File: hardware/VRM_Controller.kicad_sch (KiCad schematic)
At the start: 11 parts, among them U2001 TPS536C7B1RSLT

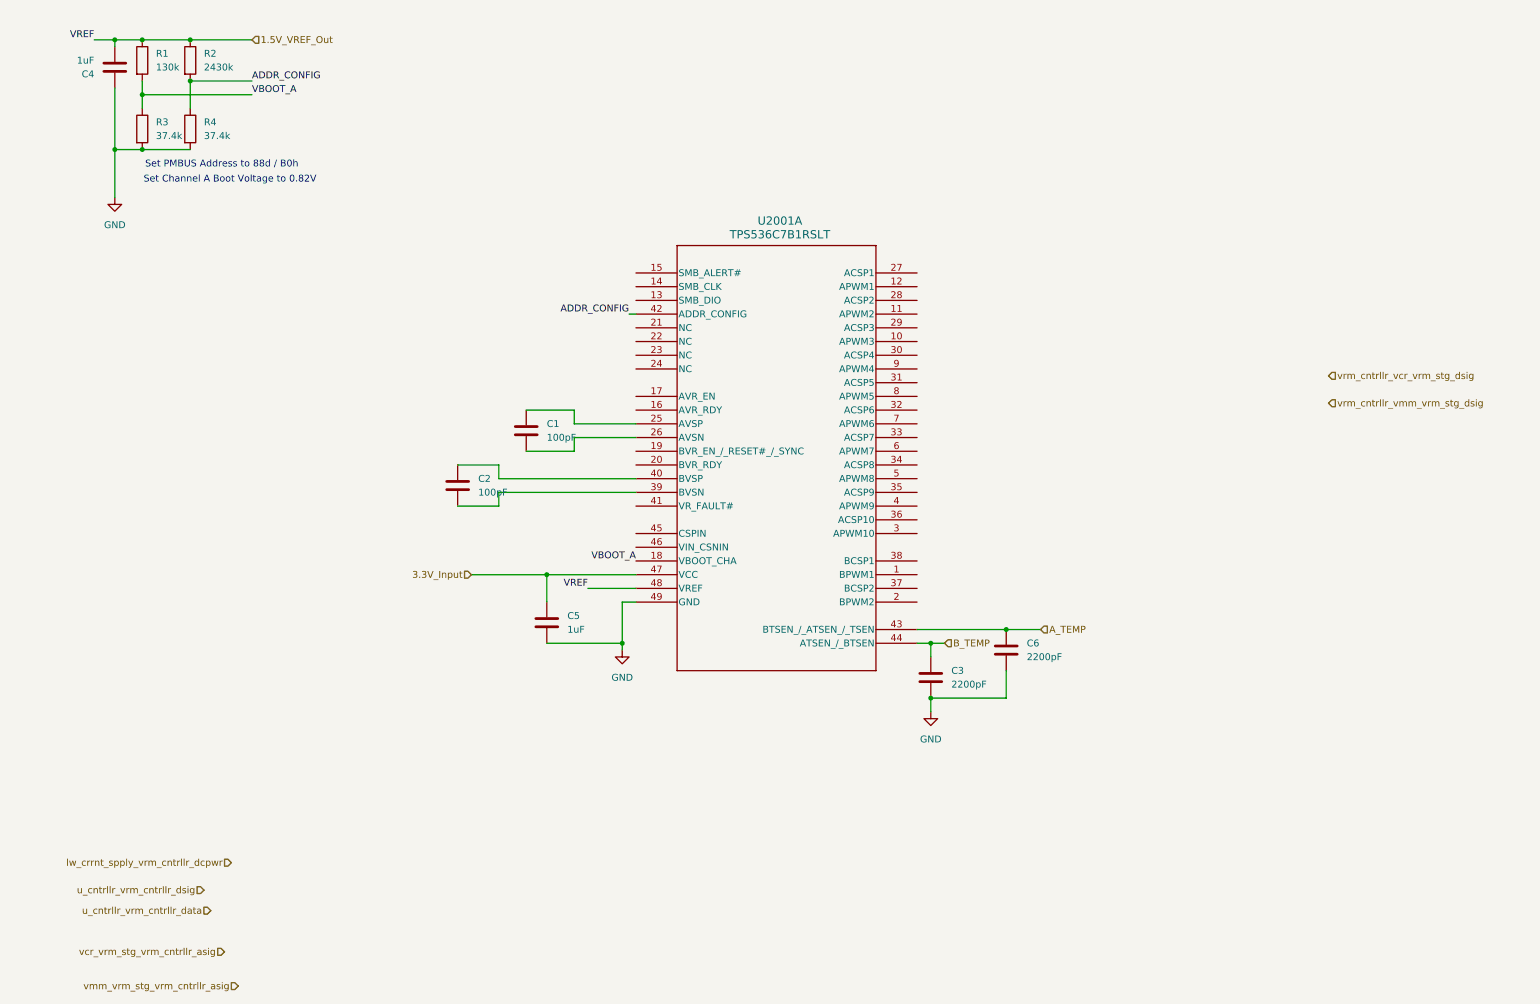
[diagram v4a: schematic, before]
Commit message: feat(schematic): VRM Controller Design
- 12v Current Sense
- Digital I/O
- MOSFET I/0
- etc
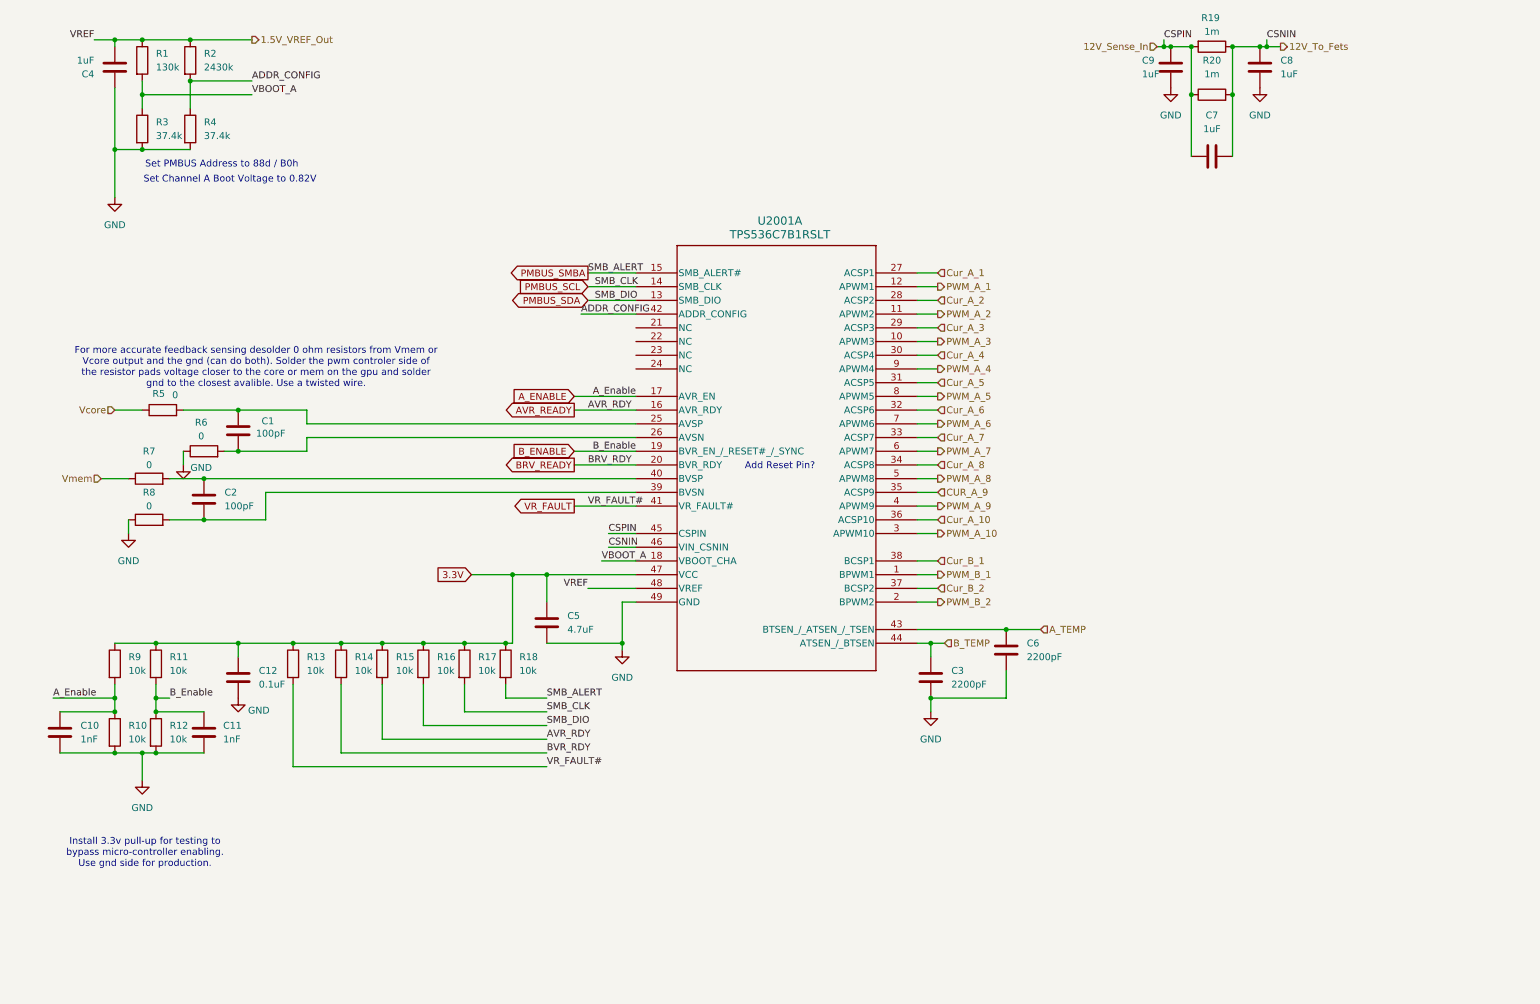
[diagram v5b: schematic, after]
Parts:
- added C10, C11: 1nF, Capacitor_SMD:C_0805_2012Metric, symbol Device:C
- added C12: 0.1uF, Capacitor_SMD:C_0805_2012Metric, symbol Device:C
- added C7, C8, C9: 1uF, Capacitor_SMD:C_0805_2012Metric, symbol Device:C
- added R10, R11, R12, R13, R14, R15, R16, R17, R18, R9: 10k, Resistor_SMD:R_0805_2012Metric, symbol Device:R
- added R19, R20: 1m, Resistor_SMD:R_Shunt_Vishay_WSK2512_6332Metric_T1.19mm, symbol Device:R
- added R5, R6, R7, R8: 0, Resistor_SMD:R_2512_6332Metric_Pad1.40x3.35mm_HandSolder, symbol Device:R
- C1, C2, C3, C4, C6: footprint (none) -> Capacitor_SMD:C_0805_2012Metric
- C5: value 1uF -> 4.7uF; footprint (none) -> Capacitor_SMD:C_0805_2012Metric
- R1, R2, R3, R4: footprint (none) -> Resistor_SMD:R_0805_2012Metric
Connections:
- net GND: now also C10.2, C11.2, C12.2, C8.2, C9.2, R10.2, R12.2, R6.1, R8.1
- net at C1.1, U2001.25 (AVSP): now also R5.2
- net at C1.2, U2001.26 (AVSN): now also R6.2
- net at C2.1, U2001.40 (BVSP): now also R7.2
- net at C2.2, U2001.39 (BVSN): now also R8.2
- net PWM_B_1: now reaches U2001.1 (BPWM1)
- net PWM_A_3: now reaches U2001.10 (APWM3)
- net PWM_A_2: now reaches U2001.11 (APWM2)
- net PWM_A_1: now reaches U2001.12 (APWM1)
- net PMBUS_SDA: now reaches U2001.13 (SMB_DIO)
- net PMBUS_SDA: now also R16.2
- net PMBUS_SCL: now reaches U2001.14 (SMB_CLK)
- net PMBUS_SCL: now also R17.2
- net PMBUS_SMBA: now reaches U2001.15 (SMB_ALERT#)
- net PMBUS_SMBA: now also R18.2
- net AVR_READY: now reaches U2001.16 (AVR_RDY)
- net AVR_READY: now also R15.2
- net A_ENABLE: now reaches U2001.17 (AVR_EN)
- net A_ENABLE: now also C10.1, R10.1, R9.2
- net B_ENABLE: now reaches U2001.19 (BVR_EN_/_RESET#_/_SYNC)
- net B_ENABLE: now also C11.1, R11.2, R12.1
- net PWM_B_2: now reaches U2001.2 (BPWM2)
- net BRV_READY: now reaches U2001.20 (BVR_RDY)
- net Cur_A_1: now reaches U2001.27 (ACSP1)
- net Cur_A_2: now reaches U2001.28 (ACSP2)
- net Cur_A_3: now reaches U2001.29 (ACSP3)
- net PWM_A_10: now reaches U2001.3 (APWM10)
- net Cur_A_4: now reaches U2001.30 (ACSP4)
- net Cur_A_5: now reaches U2001.31 (ACSP5)
- net Cur_A_6: now reaches U2001.32 (ACSP6)
- net Cur_A_7: now reaches U2001.33 (ACSP7)
- net Cur_A_8: now reaches U2001.34 (ACSP8)
- net CUR_A_9: now reaches U2001.35 (ACSP9)
- net Cur_A_10: now reaches U2001.36 (ACSP10)
- net Cur_B_2: now reaches U2001.37 (BCSP2)
- net Cur_B_1: now reaches U2001.38 (BCSP1)
- net PWM_A_9: now reaches U2001.4 (APWM9)
- net VR_FAULT: now reaches U2001.41 (VR_FAULT#)
- net VR_FAULT: now also R13.2
- net 12V_Sense_In: now reaches U2001.45 (CSPIN)
- net 12V_Sense_In: now also C7.1, C9.1, R19.2, R20.1
- net 12V_To_Fets: now reaches U2001.46 (VIN_CSNIN)
- net 12V_To_Fets: now also C7.2, C8.1, R19.1, R20.2
- net PWM_A_8: now reaches U2001.5 (APWM8)
- net PWM_A_7: now reaches U2001.6 (APWM7)
- net PWM_A_6: now reaches U2001.7 (APWM6)
- net PWM_A_5: now reaches U2001.8 (APWM5)
- net PWM_A_4: now reaches U2001.9 (APWM4)
- net 3.3V_Input renamed 3.3V
- net 3.3V: now also C12.1, R11.1, R13.1, R14.1, R15.1, R16.1, R17.1, R18.1, R9.1
- new net BVR_RDY: R14.2
- new net Vcore: R5.1
- new net Vmem: R7.1
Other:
- note added: "Add Reset Pin?"
- note added: "For more accurate feedback sensing desolder 0 ohm resistors from Vmem or Vcore output and the gnd (can do both). Solder the pwm controler side of the resistor pads voltage closer to the core or mem on the gpu and solder gnd to the closest avalible. Use a twisted wire."
- note added: "Install 3.3v pull-up for testing to bypass micro-controller enabling. Use gnd side for production."
- moved on the sheet: C1, C2

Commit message: feet(schematic): Vcore schematic made
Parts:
- U2001: footprint QFN48_6X6_TEX -> work:QFN48_6X6_TEX
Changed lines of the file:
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@@
 			)
 		)
-		(property "Footprint" "QFN48_6X6_TEX"
+		(property "Footprint" "work:QFN48_6X6_TEX"
 			(at 148.59 88.9 0)
 			(effects

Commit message: feat(schematic): Vmem schematic completed, connected controler and stages on main
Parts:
- renumbered C10 to C2001, C4 to C2002, C2 to C2003, C11 to C2004, C1 to C2005, C12 to C2006, C5 to C2007, C3 to C2008, C6 to C2009, C9 to C2010, C7 to C2011, C8 to C2012, R9 to R2001, R10 to R2002, R1 to R2003, R3 to R2004, R7 to R2005, R8 to R2006, R11 to R2007, R12 to R2008, R5 to R2009, R2 to R2010, R4 to R2011, R6 to R2012, R13 to R2013, R14 to R2014, R15 to R2015, R16 to R2016, R17 to R2017, R18 to R2018, R19 to R2019, R20 to R2020

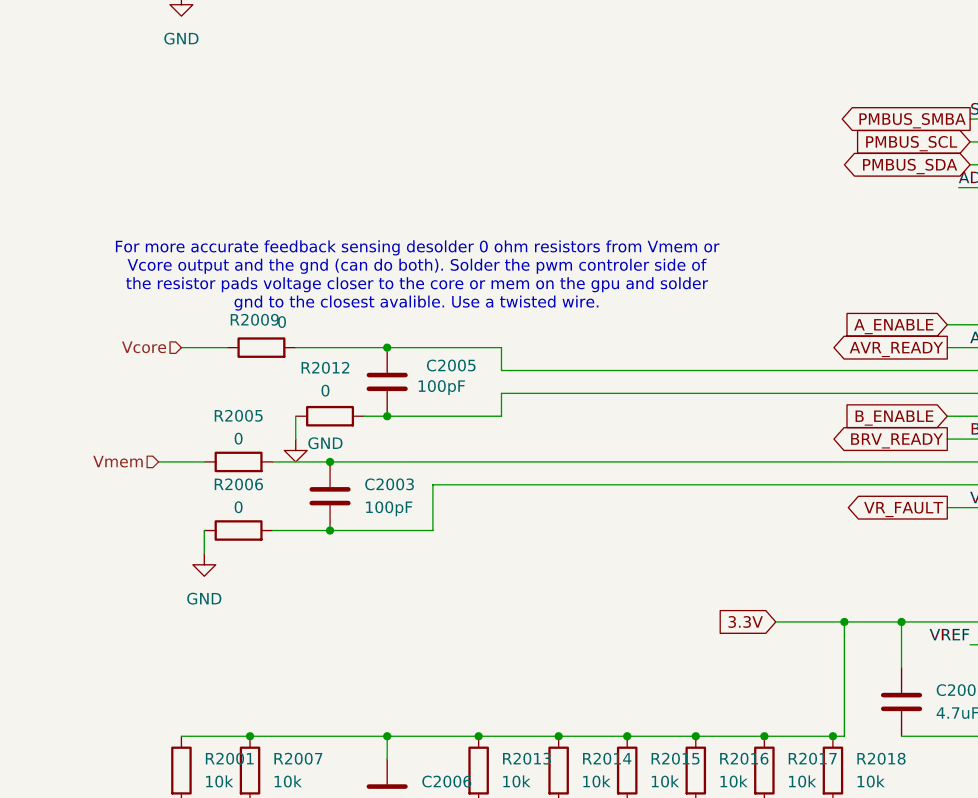
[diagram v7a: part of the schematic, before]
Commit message: feat(schematic): add feedback pins
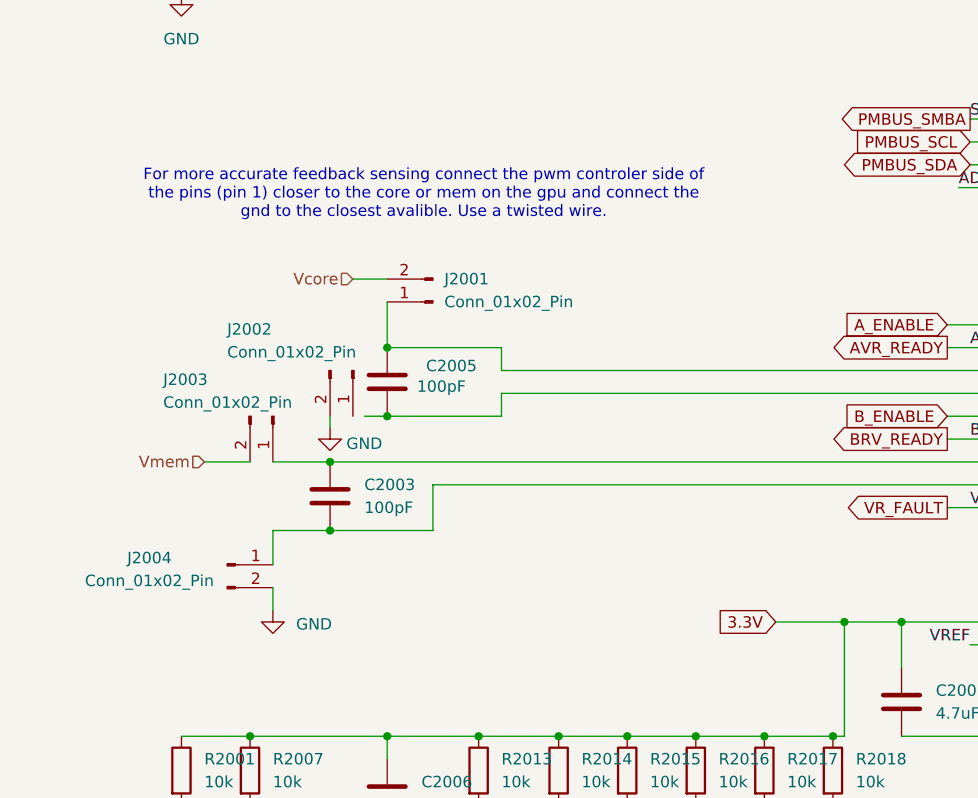
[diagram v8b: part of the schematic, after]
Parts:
- removed R2005, R2006, R2009, R2012: 0, Resistor_SMD:R_2512_6332Metric_Pad1.40x3.35mm_HandSolder, symbol Device:R
- added J2001, J2002, J2003, J2004: Conn_01x02_Pin, Connector_PinHeader_2.54mm:PinHeader_1x02_P2.54mm_Vertical, symbol Connector:Conn_01x02_Pin
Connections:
- net GND: now also J2002.2 (Pin_2), J2004.2 (Pin_2)
- net Vcore: now also J2001.2 (Pin_2)
- net Vmem: now also J2003.2 (Pin_2)
- net at C2003.1, U2001.40 (BVSP): now also J2003.1 (Pin_1)
- net at C2005.1, U2001.25 (AVSP): now also J2001.1 (Pin_1)
- net at C2003.2, U2001.39 (BVSN): now also J2004.1 (Pin_1)
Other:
- note added: "For more accurate feedback sensing connect the pwm controler side of the pins (pin 1) closer to the core or mem on the gpu and connect the gnd to the closest avalible. Use a twisted wire."
- note removed: "For more accurate feedback sensing desolder 0 ohm resistors from Vmem or Vcore output and the gnd (can do both). Solder the pwm controler side of the resistor pads voltage closer to the core or mem on the gpu and solder gnd to the closest avalible. Use a twisted wire."
